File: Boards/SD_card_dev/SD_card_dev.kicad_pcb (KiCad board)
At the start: 2 copper layers, 100.3 x 31.2 mm, 49 parts, among them J1 Barrel_jack, J2 CONN_02X03, J3 CONN_01X03, J4 SD_socket, J5 CONN_01X03, Q1 SSM3K333R, U1 LM3480, U2 ATMEGA16M1, U3 TXB0104, Y1 Crystal_SMD

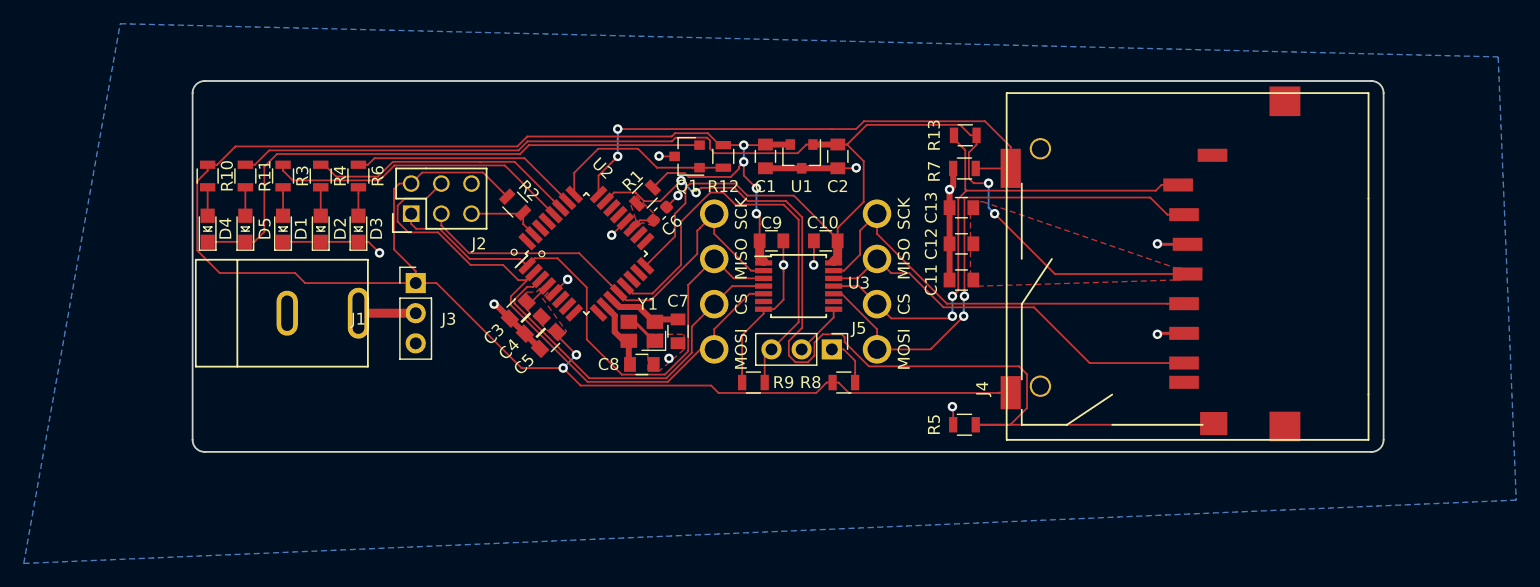
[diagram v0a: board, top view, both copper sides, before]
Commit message: updated silk stuff and board size
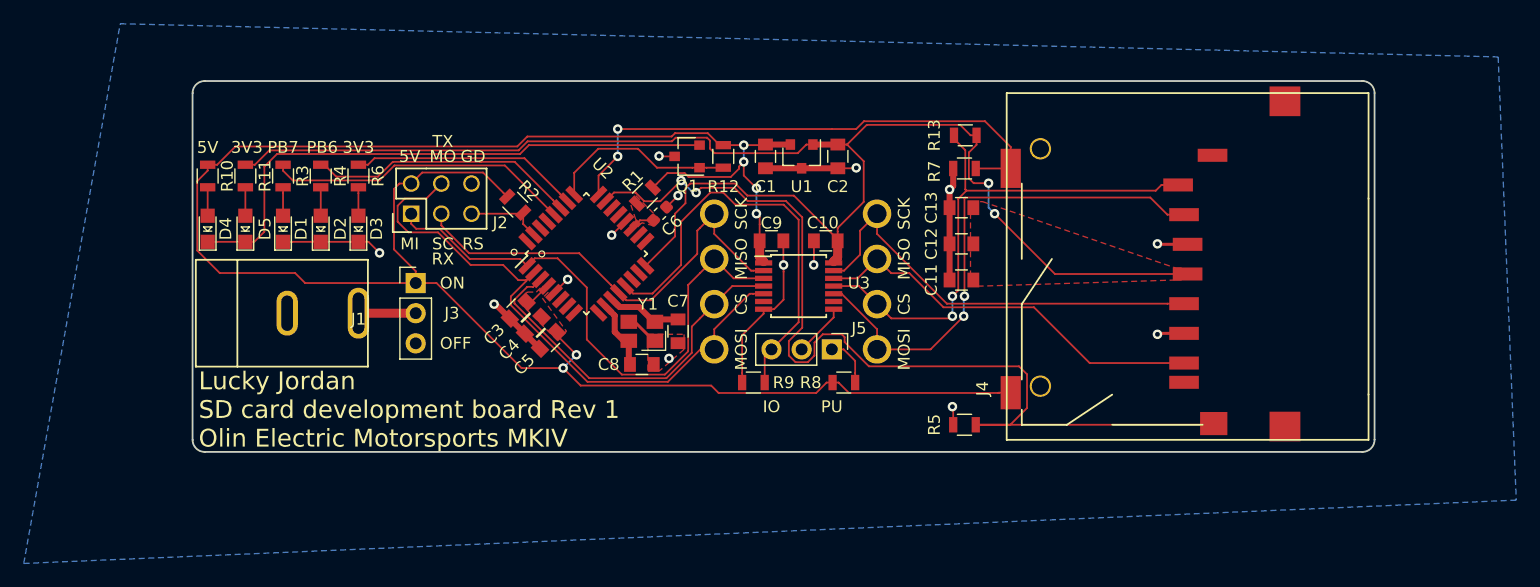
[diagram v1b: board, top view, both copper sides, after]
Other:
- board size 100.3 x 31.2 mm -> 99.6 x 31.2 mm
- board text added: "3V3"
- board text added: "5V"
- board text added: "GD"
- board text added: "IO"
- board text added: "If you plant a light bulb in your garden, does it grow into a power plant?"
- board text added: "Lucky Jordan SD card development board Rev 1 Olin Electric Motorsports MKIV"
- board text added: "MI"
- board text added: "MO"
- board text added: "OFF"
- board text added: "ON"
- board text added: "PB6"
- board text added: "PB7"
- board text added: "PU"
- board text added: "RS"
- board text added: "RX"
- board text added: "SC"
- board text added: "TX"
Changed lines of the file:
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@@
   (general
     (thickness 1.6)
-    (drawings 8)
+    (drawings 28)
     (tracks 419)
     (zones 0)
@@
       (drillshape 0)
       (scaleselection 1)
-      (outputdirectory ""))
+      (outputdirectory "gerbers/"))
   )
   (net 0 "")
@@
     (fp_line (start -0.8 -0.4) (end 0.8 -0.4) (layer F.Fab) (width 0.1))
     (fp_line (start -0.8 0.4) (end -0.8 -0.4) (layer F.Fab) (width 0.1))
-    (pad 2 smd roundrect (at 0.7875 0 45) (size 0.875 0.95) (layers F.Cu F.Paste F.Mask) (roundrect_rratio 0.25)
-      (net 1 GND))
-    (pad 1 smd roundrect (at -0.7875 0 45) (size 0.875 0.95) (layers F.Cu F.Paste F.Mask) (roundrect_rratio 0.25)
+    (pad 2 smd roundrect (at 0.787501 0 45) (size 0.875 0.95) (layers F.Cu F.Paste F.Mask) (roundrect_rratio 0.25)
+      (net 1 GND))
+    (pad 1 smd roundrect (at -0.787501 0 45) (size 0.875 0.95) (layers F.Cu F.Paste F.Mask) (roundrect_rratio 0.25)
       (net 4 /AVCC))
     (model ${KISYS3DMOD}/Capacitor_SMD.3dshapes/C_0603_1608Metric.wrl
@@
     (descr "Through hole pin header")
     (tags "pin header")
-    (fp_text reference J2 (at -2.54 5.715 180) (layer F.SilkS)
+    (fp_text reference J2 (at -0.762 7.493 180) (layer F.SilkS)
       (effects (font (size 1 1) (thickness 0.15)))
     )
@@
     (descr "Through hole straight pin header, 1x03, 2.54mm pitch, single row")
     (tags "Through hole pin header THT 1x03 2.54mm single row")
-    (fp_text reference J3 (at 2.794 3.048) (layer F.SilkS)
+    (fp_text reference J3 (at 3.048 2.54) (layer F.SilkS)
       (effects (font (size 1 1) (thickness 0.15)))
     )
@@
     (fp_line (start 1 0.62) (end -1 0.62) (layer F.Fab) (width 0.1))
     (fp_line (start -1 0.62) (end -1 -0.62) (layer F.Fab) (width 0.1))
-    (pad 2 smd rect (at 0.95 0 315) (size 0.7 1.3) (layers F.Cu F.Paste F.Mask)
+    (pad 2 smd rect (at 0.949999 0 315) (size 0.7 1.3) (layers F.Cu F.Paste F.Mask)
       (net 17 /RESET))
-    (pad 1 smd rect (at -0.95 0 315) (size 0.7 1.3) (layers F.Cu F.Paste F.Mask)
+    (pad 1 smd rect (at -0.949999 0 315) (size 0.7 1.3) (layers F.Cu F.Paste F.Mask)
       (net 2 +5V))
     (model "/home/josh/Formula/OEM_Preferred_Parts/3DModels/WRL Files/res0805.wrl"
@@
     )
   )
+  (dimension 99.822 (width 0.3) (layer Dwgs.User)
+    (gr_text "99.822 mm" (at 118.491 123.004) (layer Dwgs.User)
+      (effects (font (size 1.5 1.5) (thickness 0.3)))
+    )
+    (feature1 (pts (xy 168.402 116.586) (xy 168.402 121.490421)))
+    (feature2 (pts (xy 68.58 116.586) (xy 68.58 121.490421)))
+    (crossbar (pts (xy 68.58 120.904) (xy 168.402 120.904)))
+    (arrow1a (pts (xy 168.402 120.904) (xy 167.275496 121.490421)))
+    (arrow1b (pts (xy 168.402 120.904) (xy 167.275496 120.317579)))
+    (arrow2a (pts (xy 68.58 120.904) (xy 69.706504 121.490421)))
+    (arrow2b (pts (xy 68.58 120.904) (xy 69.706504 120.317579)))
+  )
+  (gr_text "If you plant a light bulb in your garden,\ndoes it grow into a power plant?" (at 107.696 113.284) (layer B.SilkS)
+    (effects (font (size 1.5 1.5) (thickness 0.3)) (justify mirror))
+  )
+  (gr_text PU (at 122.428 112.776) (layer F.SilkS)
+    (effects (font (size 1 1) (thickness 0.15)))
+  )
+  (gr_text IO (at 117.348 112.776) (layer F.SilkS)
+    (effects (font (size 1 1) (thickness 0.15)))
+  )
+  (gr_text TX (at 89.662 90.424) (layer F.SilkS)
+    (effects (font (size 1 1) (thickness 0.15)))
+  )
+  (gr_text RX (at 89.662 100.33) (layer F.SilkS)
+    (effects (font (size 1 1) (thickness 0.15)))
+  )
+  (gr_text RS (at 92.202 99.06) (layer F.SilkS)
+    (effects (font (size 1 1) (thickness 0.15)))
+  )
+  (gr_text SC (at 89.662 99.06) (layer F.SilkS)
+    (effects (font (size 1 1) (thickness 0.15)))
+  )
+  (gr_text MI (at 86.868 99.06) (layer F.SilkS)
+    (effects (font (size 1 1) (thickness 0.15)))
+  )
+  (gr_text GD (at 92.202 91.694) (layer F.SilkS)
+    (effects (font (size 1 1) (thickness 0.15)))
+  )
+  (gr_text MO (at 89.662 91.694) (layer F.SilkS)
+    (effects (font (size 1 1) (thickness 0.15)))
+  )
+  (gr_text 5V (at 86.868 91.694) (layer F.SilkS)
+    (effects (font (size 1 1) (thickness 0.15)))
+  )
+  (gr_text OFF (at 89.408 107.442) (layer F.SilkS)
+    (effects (font (size 1 1) (thickness 0.15)) (justify left))
+  )
+  (gr_text ON (at 89.408 102.362) (layer F.SilkS)
+    (effects (font (size 1 1) (thickness 0.15)) (justify left))
+  )
+  (gr_text 3V3 (at 82.55 90.932) (layer F.SilkS)
+    (effects (font (size 1 1) (thickness 0.15)))
+  )
+  (gr_text PB6 (at 79.502 90.932) (layer F.SilkS)
+    (effects (font (size 1 1) (thickness 0.15)))
+  )
+  (gr_text PB7 (at 76.2 90.932) (layer F.SilkS)
+    (effects (font (size 1 1) (thickness 0.15)))
+  )
+  (gr_text 3V3 (at 73.152 90.932) (layer F.SilkS)
+    (effects (font (size 1 1) (thickness 0.15)))
+  )
+  (gr_text 5V (at 69.85 90.932) (layer F.SilkS)
+    (effects (font (size 1 1) (thickness 0.15)))
+  )
+  (gr_text "Lucky Jordan\nSD card development board Rev 1\nOlin Electric Motorsports MKIV" (at 69.088 113.03) (layer F.SilkS)
+    (effects (font (size 1.5 1.5) (thickness 0.3)) (justify left))
+  )
   (gr_line (start 68.58 115.57) (end 68.58 86.36) (layer Edge.Cuts) (width 0.15))
-  (gr_line (start 167.894 116.586) (end 69.596 116.586) (layer Edge.Cuts) (width 0.15))
-  (gr_line (start 168.91 86.36) (end 168.91 115.57) (layer Edge.Cuts) (width 0.15))
-  (gr_line (start 69.596 85.344) (end 167.894 85.344) (layer Edge.Cuts) (width 0.15))
+  (gr_line (start 167.132 116.586) (end 69.596 116.586) (layer Edge.Cuts) (width 0.15))
+  (gr_line (start 168.148 86.36) (end 168.148 115.57) (layer Edge.Cuts) (width 0.15))
+  (gr_line (start 69.596 85.344) (end 167.132 85.344) (layer Edge.Cuts) (width 0.15))
   (gr_arc (start 69.596 86.36) (end 69.596 85.344) (angle -90) (layer Edge.Cuts) (width 0.15))
   (gr_arc (start 69.596 115.57) (end 68.58 115.57) (angle -90) (layer Edge.Cuts) (width 0.15))
-  (gr_arc (start 167.894 115.57) (end 167.894 116.586) (angle -90) (layer Edge.Cuts) (width 0.15))
-  (gr_arc (start 167.894 86.36) (end 168.91 86.36) (angle -90) (layer Edge.Cuts) (width 0.15))
+  (gr_arc (start 167.132 115.57) (end 167.132 116.586) (angle -90) (layer Edge.Cuts) (width 0.15))
+  (gr_arc (start 167.132 86.36) (end 168.148 86.36) (angle -90) (layer Edge.Cuts) (width 0.15))
   (via (at 108.712 108.712) (size 0.8) (drill 0.4) (layers F.Cu B.Cu) (net 1))
   (segment (start 107.426 107.226) (end 107.526 107.226) (width 0.254) (layer F.Cu) (net 1))
@@
   (segment (start 116.684 104.9434) (end 114.874 106.7534) (width 0.1524) (layer F.Cu) (net 1))
   (segment (start 116.684 104.566) (end 116.684 104.9434) (width 0.1524) (layer F.Cu) (net 1))
-  (via (at 110.998 94.742) (size 0.8) (drill 0.4) (layers F.Cu B.Cu) (net 25))
   (segment (start 87.376 101.3596) (end 87.376 102.362) (width 0.1524) (layer F.Cu) (net 2))
   (segment (start 85.54719 99.53079) (end 87.376 101.3596) (width 0.1524) (layer F.Cu) (net 2))
@@
   (segment (start 144.152 109.1) (end 152.1 109.1) (width 0.1524) (layer F.Cu) (net 22))
   (segment (start 139.45681 104.40481) (end 144.152 109.1) (width 0.1524) (layer F.Cu) (net 22))
+  (via (at 110.998 94.742) (size 0.8) (drill 0.4) (layers F.Cu B.Cu) (net 25))
   (segment (start 154.5 114.3) (end 154.6 114.2) (width 0.1524) (layer F.Cu) (net 25))
   (segment (start 134.554 114.3) (end 154.5 114.3) (width 0.1524) (layer F.Cu) (net 25))
